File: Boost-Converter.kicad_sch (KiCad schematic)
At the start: 29 parts, among them Q3 BSC047N08NS3 G, Q4 AOD66920, U3 LTC3769-QFN

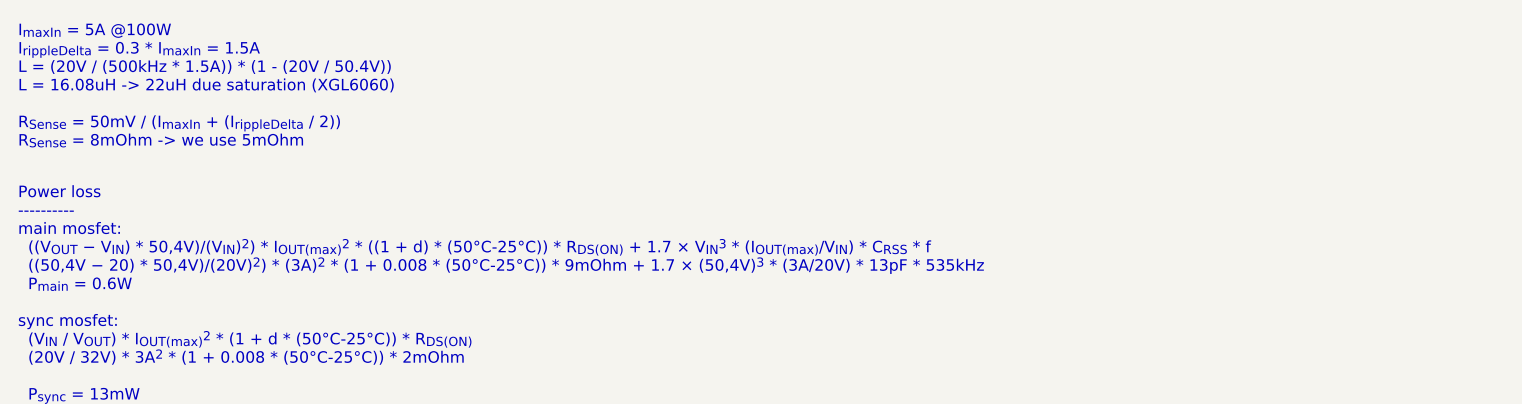
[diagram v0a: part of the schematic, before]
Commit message: Add notes for lower switching frequency
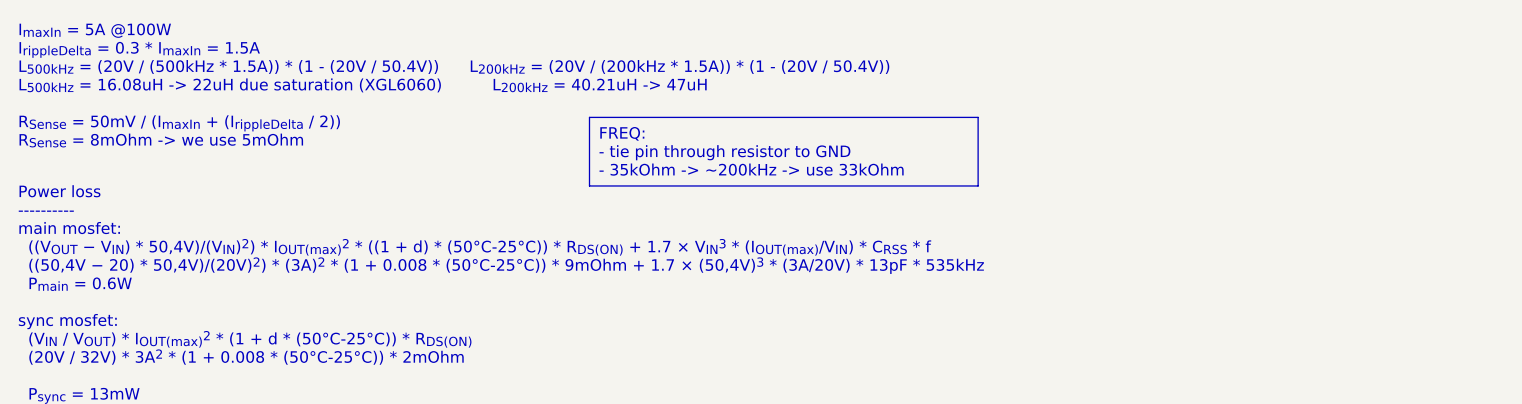
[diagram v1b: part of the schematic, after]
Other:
- note added: "I_{maxIn} = 5A @100W I_{rippleDelta} = 0.3 * I_{maxIn} = 1.5A L_{500kHz} = (20V / (500kHz * 1.5A)) * (1 - (20V / 50.4V)) L_{200kHz} = (20V / (200kHz * 1.5A)) * (1 - (20V / 50.4V)) L_{500kHz} = 16.08uH -> 22uH due saturation (XGL6060) L_{200kHz} = 40.21uH -> 47uH R_{Sense} = 50mV / (I_{maxIn} + (I_{rippleDelta} / 2)) R_{Sense} = 8mOhm -> we use 5mOhm"
- note removed: "I_{maxIn} = 5A @100W I_{rippleDelta} = 0.3 * I_{maxIn} = 1.5A L = (20V / (500kHz * 1.5A)) * (1 - (20V / 50.4V)) L = 16.08uH -> 22uH due saturation (XGL6060) R_{Sense} = 50mV / (I_{maxIn} + (I_{rippleDelta} / 2)) R_{Sense} = 8mOhm -> we use 5mOhm"
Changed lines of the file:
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@@
     (stroke (width 0) (type default))
+  )
+  (text_box "FREQ: \n- tie pin through resistor to GND\n- 35kOhm -> ~200kHz -> use 33kOhm"
+    (at 77.47 24.13 0) (size 43.18 7.62)
+    (stroke (width 0) (type default))
+    (fill (type none))
+    (effects (font (size 1.27 1.27)) (justify left top))
   )
   (text "Power loss\n----------\nmain mosfet:\n  ((V_{OUT} − V_{IN}) * 50,4V)/(V_{IN})^{2}) * I_{OUT(max)}^{2} * ((1 + d) * (50°C-25°C)) * R_{DS(ON)} + 1.7 × V_{IN}^{3} * (I_{OUT(max)}/V_{IN}) * C_{RSS} * f\n  ((50,4V − 20) * 50,4V)/(20V)^{2}) * (3A)^{2} * (1 + 0.008 * (50°C-25°C)) * 9mOhm + 1.7 × (50,4V)^{3} * (3A/20V) * 13pF * 535kHz\n  P_{main} = 0.6W\n\nsync mosfet:\n  (V_{IN} / V_{OUT}) * I_{OUT(max)}^{2} * (1 + d * (50°C-25°C)) * R_{DS(ON)}\n  (20V / 32V) * 3A^{2} * (1 + 0.008 * (50°C-25°C)) * 2mOhm\n\n  P_{sync} = 13mW\n"
@@
     (effects (font (size 1.27 1.27)) (justify left bottom))
   )
-  (text "I_{maxIn} = 5A @100W\nI_{rippleDelta} = 0.3 * I_{maxIn} = 1.5A\nL = (20V / (500kHz * 1.5A)) * (1 - (20V / 50.4V))\nL = 16.08uH -> 22uH due saturation (XGL6060)\n\nR_{Sense} = 50mV / (I_{maxIn} + (I_{rippleDelta} / 2))\nR_{Sense} = 8mOhm -> we use 5mOhm \n\n\n"
+  (text "I_{maxIn} = 5A @100W\nI_{rippleDelta} = 0.3 * I_{maxIn} = 1.5A\nL_{500kHz} = (20V / (500kHz * 1.5A)) * (1 - (20V / 50.4V))      L_{200kHz} = (20V / (200kHz * 1.5A)) * (1 - (20V / 50.4V))\nL_{500kHz} = 16.08uH -> 22uH due saturation (XGL6060)          L_{200kHz} = 40.21uH -> 47uH\n\nR_{Sense} = 50mV / (I_{maxIn} + (I_{rippleDelta} / 2))\nR_{Sense} = 8mOhm -> we use 5mOhm \n\n\n"
     (at 13.97 31.75 0)
     (effects (font (size 1.27 1.27)) (justify left bottom))
